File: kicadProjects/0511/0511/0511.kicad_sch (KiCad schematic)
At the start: 13 parts, among them U1 UDA1334A_Breakout, U2 YAAJ_BlackPill, U3 MCP23017, U4 MCP23017

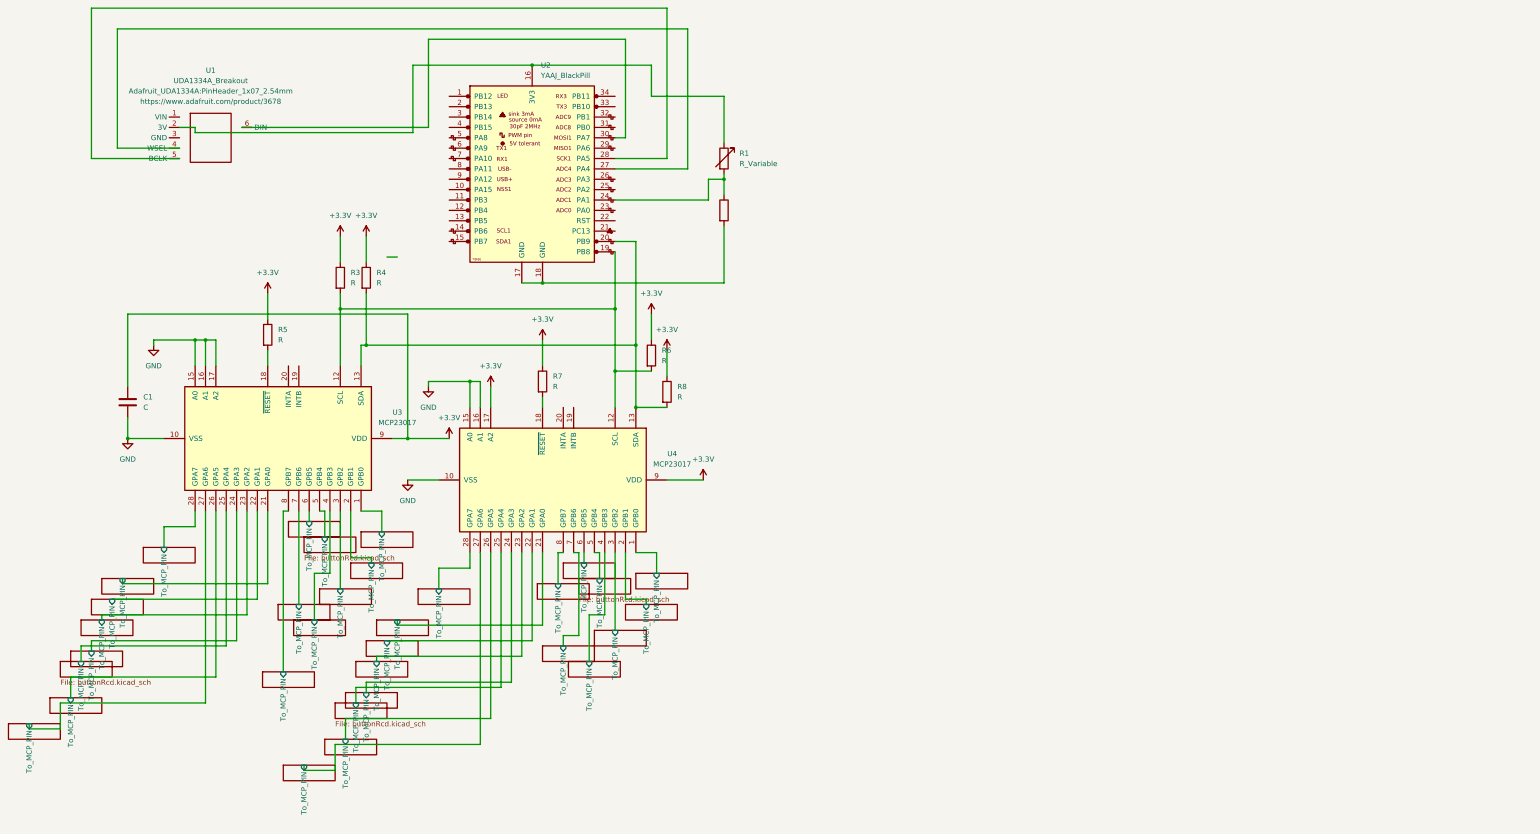
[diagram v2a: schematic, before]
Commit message: ajout 2 mcp23017
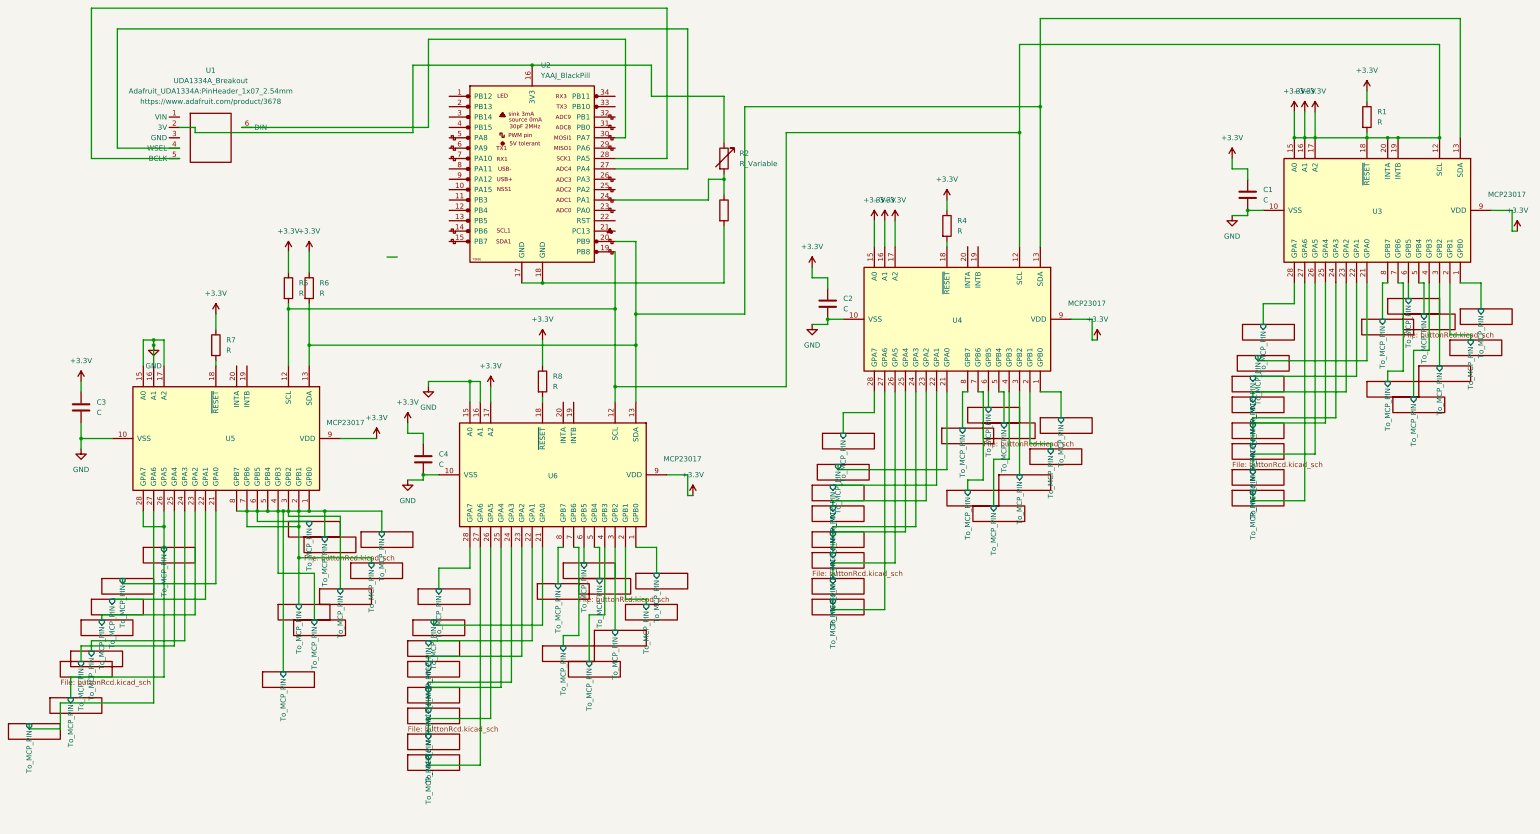
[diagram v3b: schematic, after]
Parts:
- removed R6, R8: R, symbol Device:R
- added C1, C2, C4: C, Capacitor_THT:CP_Axial_L10.0mm_D4.5mm_P15.00mm_Horizontal, symbol Device:C
- added R1, R4: R, Resistor_SMD:R_0603_1608Metric, symbol Device:R
- added U3, U4: MCP23017, Package_DIP:DIP-28_W7.62mm, symbol Stm32F411BlackPill:MCP23017
- C3: renamed from C1; footprint (none) -> Capacitor_THT:CP_Axial_L10.0mm_D4.5mm_P15.00mm_Horizontal
- R5: renamed from R3; footprint (none) -> Resistor_SMD:R_0603_1608Metric
- R6: renamed from R4; footprint (none) -> Resistor_SMD:R_0603_1608Metric
- R7: renamed from R5; footprint (none) -> Resistor_SMD:R_0603_1608Metric
- R8: renamed from R7; footprint (none) -> Resistor_SMD:R_0603_1608Metric
- renumbered R1 to R2, R2 to R3, U3 to U5, U4 to U6
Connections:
- net Button_RCD11/To_MCP_PIN is gone; now on net Button_RCD10/To_MCP_PIN: U5.3 (GPB2)
- net Button_RCD12/To_MCP_PIN is gone; now on net Button_RCD10/To_MCP_PIN: U5.2 (GPB1)
- net Button_RCD13/To_MCP_PIN is gone; now on net Button_RCD10/To_MCP_PIN: U5.1 (GPB0)
- net Button_RCD14/To_MCP_PIN is gone; now on net Button_RCD1/To_MCP_PIN: U5.28 (GPA7)
- net Button_RCD15/To_MCP_PIN is gone; now on net Button_RCD10/To_MCP_PIN: U5.7 (GPB6)
- net Button_RCD19/To_MCP_PIN is gone; now on net Button_RCD18/To_MCP_PIN: U6.24 (GPA3)
- net Button_RCD7/To_MCP_PIN is gone; now on net Button_RCD10/To_MCP_PIN: U5.8 (GPB7)
- net Button_RCD8/To_MCP_PIN is gone; now on net Button_RCD10/To_MCP_PIN: U5.6 (GPB5)
- net Button_RCD9/To_MCP_PIN is gone; now on net Button_RCD10/To_MCP_PIN: U5.5 (GPB4)
- net +3.3V: now also R5.2, U2.19 (PB8), U5.12 (SCL), U6.12 (SCL), C1.1, C2.1, C4.1, R1.1, R1.2, R4.1, U3.12 (SCL), U3.15 (A0), U3.16 (A1), U3.17 (A2), U3.18 (~{RESET}), U3.19 (INTB), U3.20 (INTA), U3.9 (VDD), U4.12 (SCL), U4.15 (A0), U4.16 (A1), U4.17 (A2), U4.9 (VDD)
- net GND: now also C1.2, C2.2, C4.2, U3.10 (VSS), U4.10 (VSS)
- net at R6.2, U2.20 (PB9), U5.13 (SDA)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: now also U3.13 (SDA), U4.13 (SDA)
- new net: R4.2, U4.18 (~{RESET})
- new net Button_RCD32/To_MCP_PIN: U4.27 (GPA6)
- new net Button_RCD33/To_MCP_PIN: U4.26 (GPA5)
- new net Button_RCD34/To_MCP_PIN: U4.24 (GPA3), U4.25 (GPA4)
- new net Button_RCD36/To_MCP_PIN: U4.23 (GPA2)
- new net Button_RCD37/To_MCP_PIN: U4.22 (GPA1)
- new net Button_RCD38/To_MCP_PIN: U4.21 (GPA0)
- new net Button_RCD39/To_MCP_PIN: U4.8 (GPB7)
- new net Button_RCD40/To_MCP_PIN: U4.6 (GPB5)
- new net Button_RCD41/To_MCP_PIN: U4.5 (GPB4)
- new net Button_RCD42/To_MCP_PIN: U4.4 (GPB3)
- new net Button_RCD43/To_MCP_PIN: U4.3 (GPB2)
- new net Button_RCD44/To_MCP_PIN: U4.2 (GPB1)
- new net Button_RCD45/To_MCP_PIN: U4.1 (GPB0)
- new net Button_RCD46/To_MCP_PIN: U4.28 (GPA7)
- new net Button_RCD47/To_MCP_PIN: U4.7 (GPB6)
- new net Button_RCD48/To_MCP_PIN: U3.27 (GPA6)
- new net Button_RCD49/To_MCP_PIN: U3.26 (GPA5)
- new net Button_RCD50/To_MCP_PIN: U3.24 (GPA3), U3.25 (GPA4)
- new net Button_RCD52/To_MCP_PIN: U3.23 (GPA2)
- new net Button_RCD53/To_MCP_PIN: U3.22 (GPA1)
- new net Button_RCD54/To_MCP_PIN: U3.21 (GPA0)
- new net Button_RCD55/To_MCP_PIN: U3.8 (GPB7)
- new net Button_RCD56/To_MCP_PIN: U3.6 (GPB5)
- new net Button_RCD57/To_MCP_PIN: U3.5 (GPB4)
- new net Button_RCD58/To_MCP_PIN: U3.4 (GPB3)
- new net Button_RCD59/To_MCP_PIN: U3.3 (GPB2)
- new net Button_RCD60/To_MCP_PIN: U3.2 (GPB1)
- new net Button_RCD61/To_MCP_PIN: U3.1 (GPB0)
- new net Button_RCD62/To_MCP_PIN: U3.28 (GPA7)
- new net Button_RCD63/To_MCP_PIN: U3.7 (GPB6)
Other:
- added sheet Button_RCD32 (buttonRcd.kicad_sch)
- added sheet Button_RCD33 (buttonRcd.kicad_sch)
- added sheet Button_RCD34 (buttonRcd.kicad_sch)
- added sheet Button_RCD35 (buttonRcd.kicad_sch)
- added sheet Button_RCD36 (buttonRcd.kicad_sch)
- added sheet Button_RCD37 (buttonRcd.kicad_sch)
- added sheet Button_RCD38 (buttonRcd.kicad_sch)
- added sheet Button_RCD39 (buttonRcd.kicad_sch)
- added sheet Button_RCD40 (buttonRcd.kicad_sch)
- added sheet Button_RCD41 (buttonRcd.kicad_sch)
- added sheet Button_RCD42 (buttonRcd.kicad_sch)
- added sheet Button_RCD43 (buttonRcd.kicad_sch)
- added sheet Button_RCD44 (buttonRcd.kicad_sch)
- added sheet Button_RCD45 (buttonRcd.kicad_sch)
- added sheet Button_RCD46 (buttonRcd.kicad_sch)
- added sheet Button_RCD47 (buttonRcd.kicad_sch)
- added sheet Button_RCD48 (buttonRcd.kicad_sch)
- added sheet Button_RCD49 (buttonRcd.kicad_sch)
- added sheet Button_RCD50 (buttonRcd.kicad_sch)
- added sheet Button_RCD51 (buttonRcd.kicad_sch)
- added sheet Button_RCD52 (buttonRcd.kicad_sch)
- added sheet Button_RCD53 (buttonRcd.kicad_sch)
- added sheet Button_RCD54 (buttonRcd.kicad_sch)
- added sheet Button_RCD55 (buttonRcd.kicad_sch)
- added sheet Button_RCD56 (buttonRcd.kicad_sch)
- added sheet Button_RCD57 (buttonRcd.kicad_sch)
- added sheet Button_RCD58 (buttonRcd.kicad_sch)
- added sheet Button_RCD59 (buttonRcd.kicad_sch)
- added sheet Button_RCD60 (buttonRcd.kicad_sch)
- added sheet Button_RCD61 (buttonRcd.kicad_sch)
- added sheet Button_RCD62 (buttonRcd.kicad_sch)
- added sheet Button_RCD63 (buttonRcd.kicad_sch)
- moved on the sheet: C3, R5, R6, R7, U5, U6

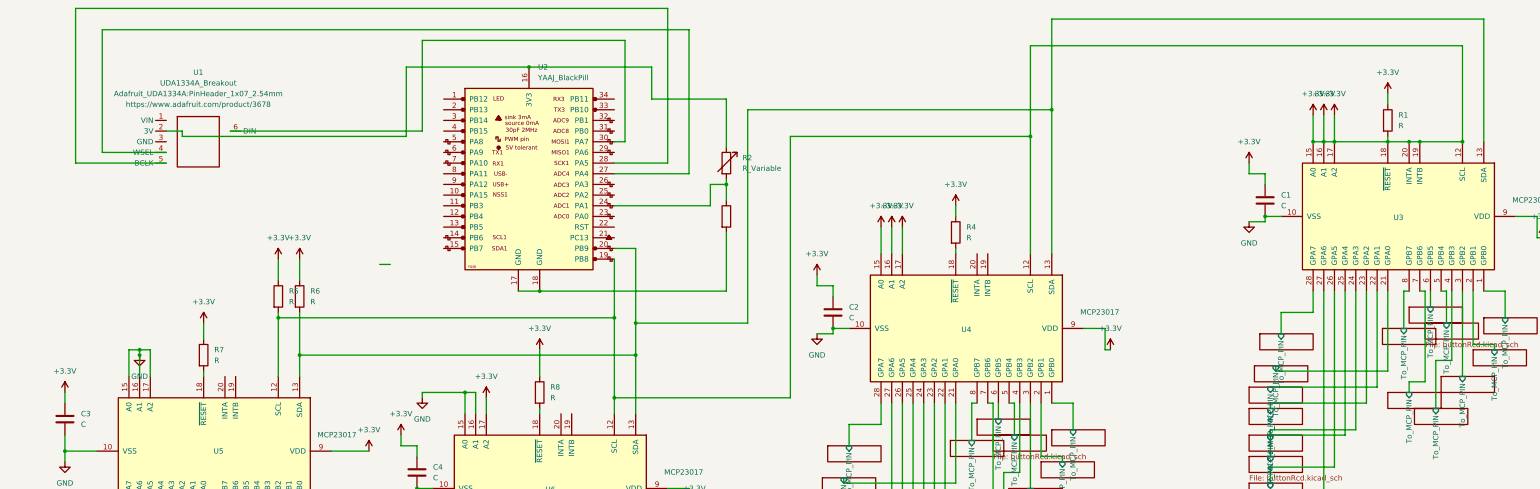
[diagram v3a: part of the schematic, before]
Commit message: correctifs connexions manquantes
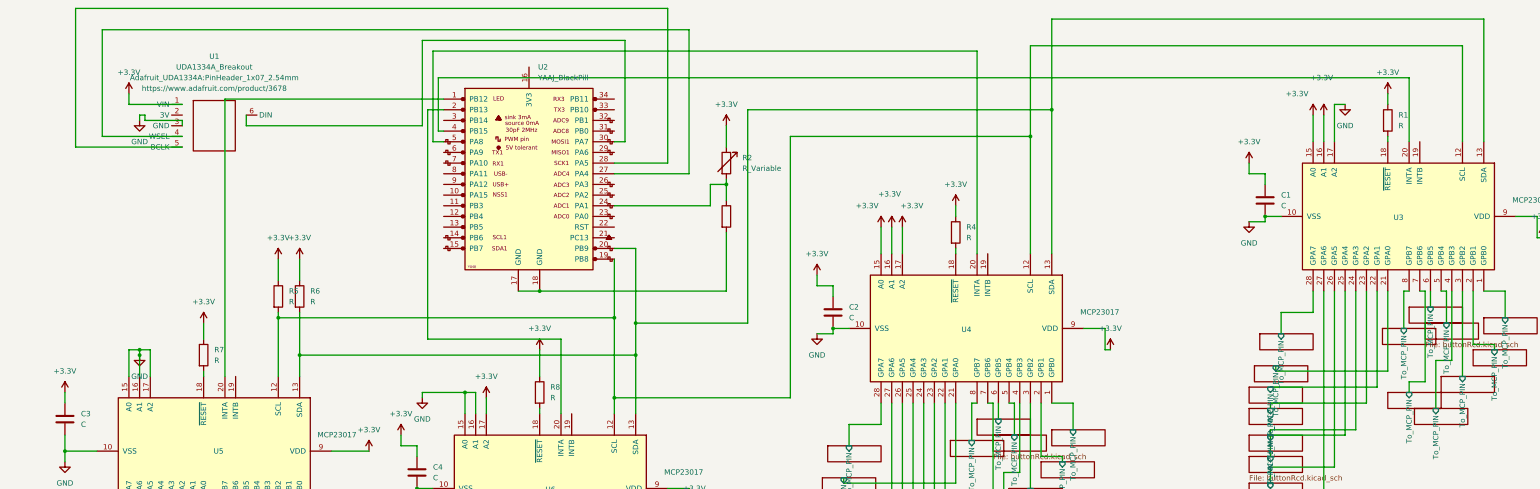
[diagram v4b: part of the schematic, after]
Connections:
- net +3.3V: now also R2.1, U1.1 (VIN); no longer R1.2, R5.2, U2.19 (PB8), U3.12 (SCL), U3.17 (A2), U3.18 (~{RESET}), U3.19 (INTB), U3.20 (INTA), U4.12 (SCL), U5.12 (SCL), U6.12 (SCL)
- net GND: now also U1.3 (GND), U3.17 (A2)
- net at U6.20 (INTA): now also U2.2 (PB13)
- net at U4.20 (INTA): now also U2.5 (PA8)
- net at U2.1 (PB12): now also U5.20 (INTA)
- net at U2.4 (PB15): now also U3.20 (INTA)
- new net: R5.2, U2.19 (PB8), U3.12 (SCL), U4.12 (SCL), U5.12 (SCL), U6.12 (SCL)
- new net: R1.2, U3.18 (~{RESET})
- now unconnected: U1.2 (3V), U2.16 (3V3)
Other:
- moved on the sheet: U1

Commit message: poursuite
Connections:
- net Button_RCD54/To_MCP_PIN is gone; now on net Button_RCD52/To_MCP_PIN: U3.21 (GPA0)
- net Button_RCD62/To_MCP_PIN is gone; now on net Button_RCD53/To_MCP_PIN: U3.28 (GPA7)
- net Button_RCD18/To_MCP_PIN: no longer U6.24 (GPA3), U6.25 (GPA4)
- net Button_RCD34/To_MCP_PIN: no longer U4.24 (GPA3), U4.25 (GPA4)
- net Button_RCD36/To_MCP_PIN: now also U4.22 (GPA1); no longer U4.23 (GPA2)
- net Button_RCD37/To_MCP_PIN: now also U4.21 (GPA0); no longer U4.22 (GPA1)
- net Button_RCD38/To_MCP_PIN: now also U4.28 (GPA7); no longer U4.21 (GPA0)
- net Button_RCD39/To_MCP_PIN: no longer U4.8 (GPB7)
- net Button_RCD46/To_MCP_PIN: now also U3.27 (GPA6); no longer U4.28 (GPA7)
- net Button_RCD48/To_MCP_PIN: now also U3.26 (GPA5); no longer U3.27 (GPA6)
- net Button_RCD49/To_MCP_PIN: no longer U3.26 (GPA5)
- net Button_RCD50/To_MCP_PIN: now also U3.23 (GPA2); no longer U3.24 (GPA3), U3.25 (GPA4)
- net Button_RCD52/To_MCP_PIN: no longer U3.23 (GPA2)
- net Button_RCD53/To_MCP_PIN: no longer U3.22 (GPA1)
- net Button_RCD/To_MCP_PIN renamed Button_RCD19/To_MCP_PIN
- net Button_RCD1/To_MCP_PIN renamed Button_RCD71/To_MCP_PIN
- net Button_RCD71/To_MCP_PIN: no longer U5.28 (GPA7)
- removed net Button_RCD10/To_MCP_PIN: U5.1 (GPB0), U5.2 (GPB1), U5.3 (GPB2), U5.4 (GPB3), U5.5 (GPB4), U5.6 (GPB5), U5.7 (GPB6), U5.8 (GPB7)
- net Button_RCD2/To_MCP_PIN renamed Button_RCD82/To_MCP_PIN
- net Button_RCD3/To_MCP_PIN renamed Button_RCD81/To_MCP_PIN
- net Button_RCD4/To_MCP_PIN renamed Button_RCD73/To_MCP_PIN
- net Button_RCD5/To_MCP_PIN renamed Button_RCD74/To_MCP_PIN
- net Button_RCD6/To_MCP_PIN renamed Button_RCD75/To_MCP_PIN
- new net Button_RCD35/To_MCP_PIN: U4.23 (GPA2)
- new net Button_RCD51/To_MCP_PIN: U3.22 (GPA1)
- new net Button_RCD64/To_MCP_PIN: U5.6 (GPB5)
- new net Button_RCD65/To_MCP_PIN: U5.5 (GPB4)
- new net Button_RCD66/To_MCP_PIN: U5.4 (GPB3)
- new net Button_RCD67/To_MCP_PIN: U5.3 (GPB2)
- new net Button_RCD68/To_MCP_PIN: U5.2 (GPB1)
- new net Button_RCD69/To_MCP_PIN: U5.1 (GPB0)
- new net Button_RCD70/To_MCP_PIN: U5.8 (GPB7)
- new net Button_RCD76/To_MCP_PIN: U5.28 (GPA7)
- new net Button_RCD79/To_MCP_PIN: U6.24 (GPA3)
- new net Button_RCD80/To_MCP_PIN: U6.25 (GPA4)
- new net Button_RCD83/To_MCP_PIN: U4.24 (GPA3)
- new net Button_RCD84/To_MCP_PIN: U4.25 (GPA4)
- new net Button_RCD85/To_MCP_PIN: U3.24 (GPA3)
- new net Button_RCD86/To_MCP_PIN: U3.25 (GPA4)
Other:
- removed sheet Button_RCD
- removed sheet Button_RCD1
- removed sheet Button_RCD10
- removed sheet Button_RCD11
- removed sheet Button_RCD12
- removed sheet Button_RCD13
- removed sheet Button_RCD14
- removed sheet Button_RCD15
- removed sheet Button_RCD2
- removed sheet Button_RCD3
- removed sheet Button_RCD4
- removed sheet Button_RCD5
- removed sheet Button_RCD54
- removed sheet Button_RCD6
- removed sheet Button_RCD62
- removed sheet Button_RCD7
- removed sheet Button_RCD8
- removed sheet Button_RCD9
- added sheet Button_RCD64 (buttonRcd.kicad_sch)
- added sheet Button_RCD65 (buttonRcd.kicad_sch)
- added sheet Button_RCD66 (buttonRcd.kicad_sch)
- added sheet Button_RCD67 (buttonRcd.kicad_sch)
- added sheet Button_RCD68 (buttonRcd.kicad_sch)
- added sheet Button_RCD69 (buttonRcd.kicad_sch)
- added sheet Button_RCD70 (buttonRcd.kicad_sch)
- added sheet Button_RCD71 (buttonRcd.kicad_sch)
- added sheet Button_RCD72 (buttonRcd.kicad_sch)
- added sheet Button_RCD73 (buttonRcd.kicad_sch)
- added sheet Button_RCD74 (buttonRcd.kicad_sch)
- added sheet Button_RCD75 (buttonRcd.kicad_sch)
- added sheet Button_RCD76 (buttonRcd.kicad_sch)
- added sheet Button_RCD79 (buttonRcd.kicad_sch)
- added sheet Button_RCD80 (buttonRcd.kicad_sch)
- added sheet Button_RCD81 (buttonRcd.kicad_sch)
- added sheet Button_RCD82 (buttonRcd.kicad_sch)
- added sheet Button_RCD83 (buttonRcd.kicad_sch)
- added sheet Button_RCD84 (buttonRcd.kicad_sch)
- added sheet Button_RCD85 (buttonRcd.kicad_sch)
- added sheet Button_RCD86 (buttonRcd.kicad_sch)

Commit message: ajout connexions manquantes
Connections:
- net GND: now also R3.2, U2.17 (GND), U2.18 (GND)
- net at U2.4 (PB15), U3.20 (INTA): now also U2.1 (PB12), U2.2 (PB13), U2.3 (PB14), U2.5 (PA8), U2.7 (PA10), U4.20 (INTA), U5.20 (INTA), U6.20 (INTA)

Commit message: adaptation empreintes mcp23017 ajout valeurs aux résistances corrections empreintes des résistances et condensateurs
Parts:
- added R1, R12, R14, R16, R2, R4, R7, R9: 10K, Resistor_SMD:R_0603_1608Metric, symbol Device:R
- added U7: CP2102N-Axx-xQFN24, Package_DFN_QFN:QFN-24-1EP_4x4mm_P0.5mm_EP2.6x2.6mm, symbol Interface_USB:CP2102N-Axx-xQFN24
- added U8: STM32F411RETx, Package_QFP:LQFP-64_10x10mm_P0.5mm, symbol MCU_ST_STM32F4:STM32F411RETx
- C1, C2, C3, C4: footprint Capacitor_THT:CP_Axial_L10.0mm_D4.5mm_P15.00mm_Horizontal -> Capacitor_SMD:C_0603_1608Metric
- R10: renamed from R5; value R -> 4,7k
- R11: renamed from R6; value R -> 4,7K
- R13: renamed from R7; value R -> 10K
- R15: renamed from R8; value R -> 10K
- R3: renamed from R1; value R -> 10K
- R6: renamed from R3; footprint Resistor_THT:R_Axial_DIN0207_L6.3mm_D2.5mm_P7.62mm_Horizontal -> Resistor_SMD:R_0603_1608Metric
- R8: renamed from R4; value R -> 10K
- U3, U4, U5, U6: footprint Package_DIP:DIP-28_W7.62mm -> Package_SO:SOIC-28W_7.5x17.9mm_P1.27mm
- renumbered R2 to R5
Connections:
- net +3.3V: now also R1.1, R12.1, R14.1, R16.1, R2.1, R4.1, R7.1, R9.1
- net SDA: now reaches R11.2, U2.20 (PB9), U3.13 (SDA), U4.13 (SDA), U5.13 (SDA), U6.13 (SDA)
- net SCL: now reaches R10.2, U2.19 (PB8), U3.12 (SCL), U4.12 (SCL), U5.12 (SCL), U6.12 (SCL)
- net at U3.19 (INTB): now also R2.2
- net at U2.1 (PB12), U2.2 (PB13), U2.3 (PB14)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: now also R1.2, R16.2, R4.2, R9.2
- net at U6.19 (INTB): now also R14.2
- net at U4.19 (INTB): now also R7.2
- net at U5.19 (INTB): now also R12.2
- new net: U8.18 (VSS), U8.31 (VSS), U8.47 (VSS), U8.63 (VSS)
- new net: U7.2 (GND), U7.25 (GND)

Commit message: poursuite
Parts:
- C1, C2, C3, C4: value C -> 0.1uF
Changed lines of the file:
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@@
 			)
 		)
-		(property "Value" "C"
+		(property "Value" "0.1uF"
 			(at 323.85 58.4199 0)
 			(effects
@@
 			)
 		)
-		(property "Value" "C"
+		(property "Value" "0.1uF"
 			(at 38.1 110.4899 0)
 			(effects
@@
 			)
 		)
-		(property "Value" "C"
+		(property "Value" "0.1uF"
 			(at 121.92 123.1899 0)
 			(effects
@@
 			)
 		)
-		(property "Value" "C"
+		(property "Value" "0.1uF"
 			(at 220.98 85.0899 0)
 			(effects
@@
 		)
 		(pin "To_MCP_PIN" input
-			(at 39.37 173.99 90)
+			(at 38.1 173.99 90)
 			(effects
 				(font
